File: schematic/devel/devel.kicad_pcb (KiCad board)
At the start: 2 copper layers, 66 parts, among them J1 CONN_PWR, J2 CONN_X1, J3 CONN_Y2, J4 CONN_X2, J5 CONN_Y1, Q1 Q_PMOS_GSD, Q2 Q_NMOS_GSD, Q3 Q_PMOS_GSD, Q4 Q_NMOS_GSD, U1 LM317_SOT223, U2 LM337_SOT223, U3 REF5010IDGK, U4 OPA4197

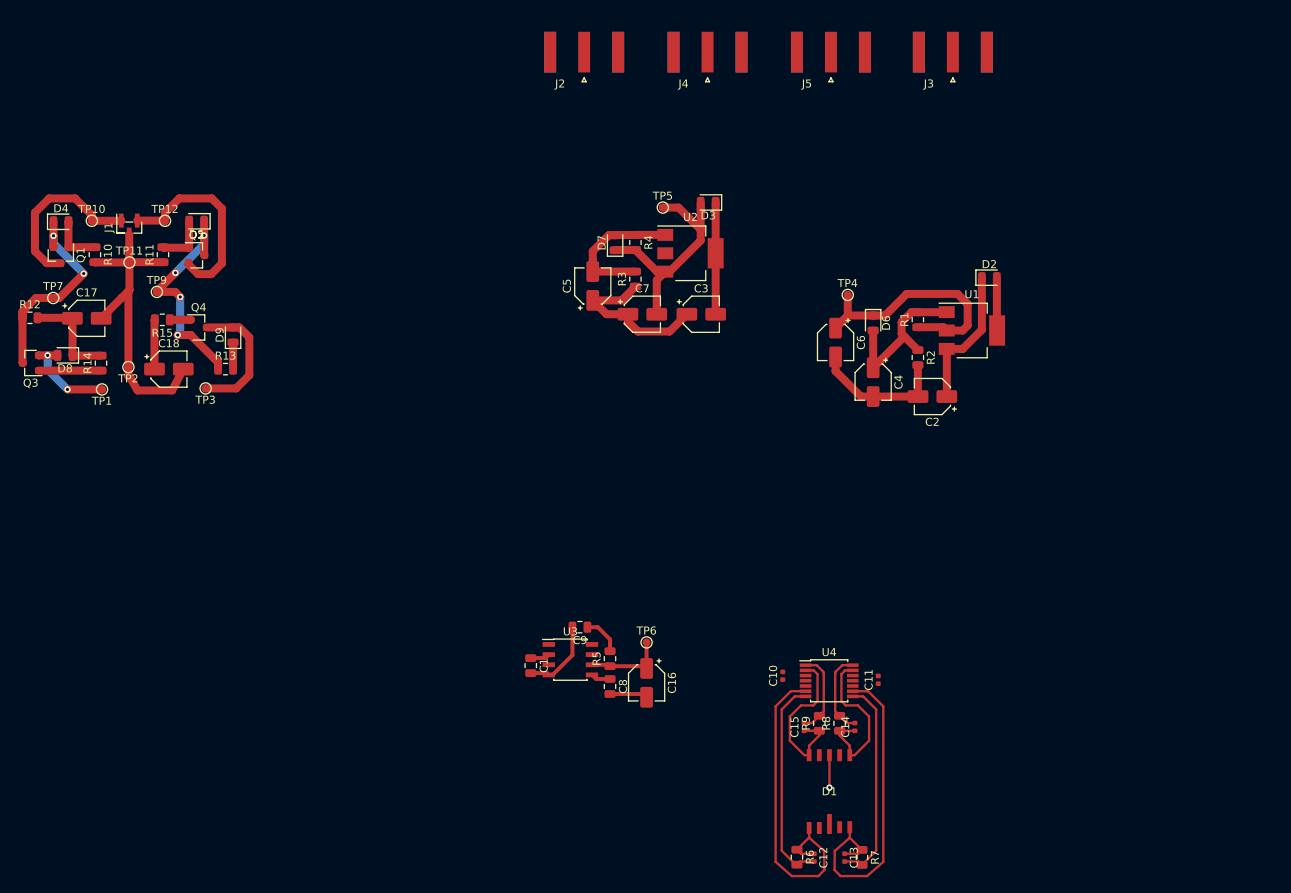
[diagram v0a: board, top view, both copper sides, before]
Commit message: retraced regulators according to datasheet layout
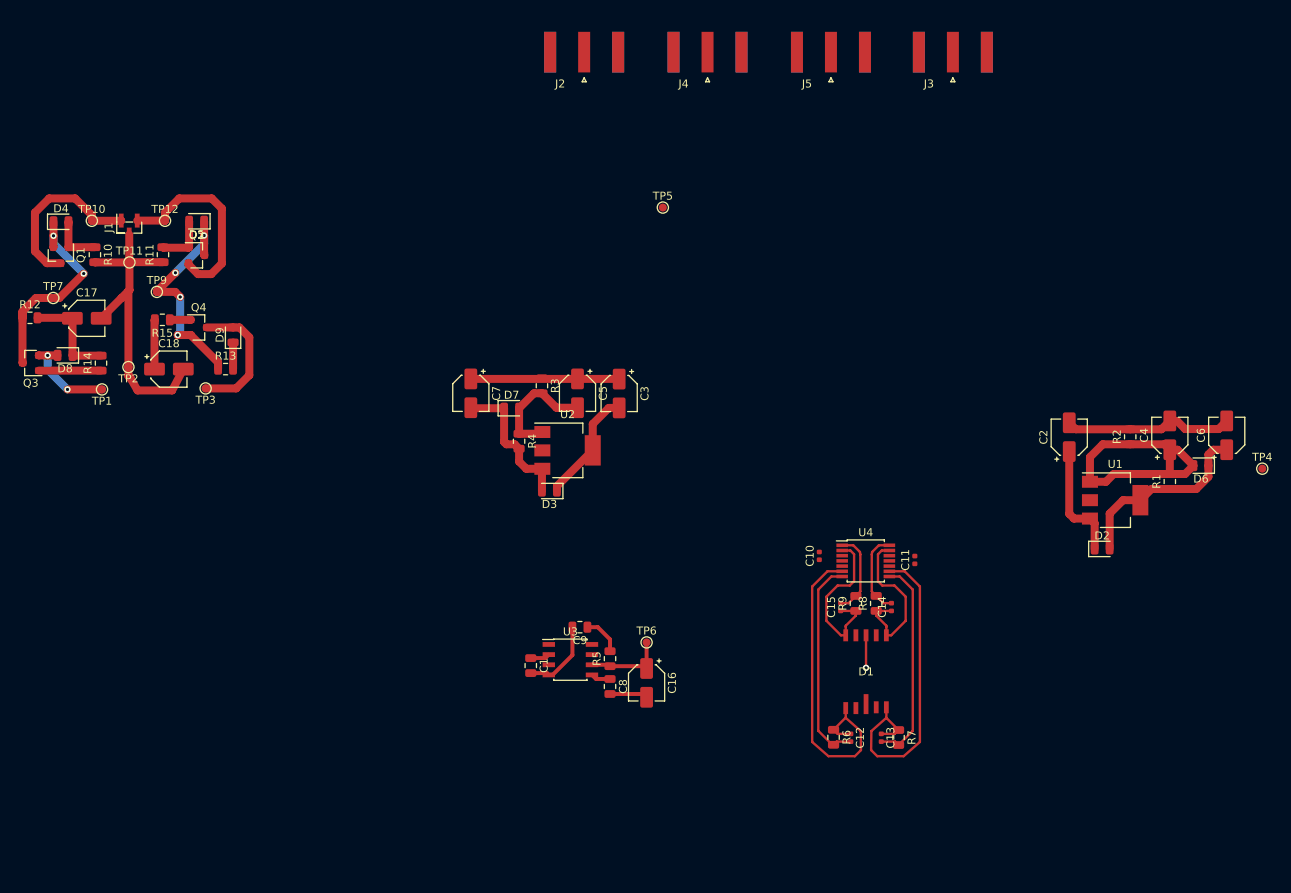
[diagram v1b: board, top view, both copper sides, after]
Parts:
- moved TP4 56.2 mm to (191.3, 125.2)
- moved C6 50.3 mm to (186.8, 121.1), turned to 90 degrees
- moved D6 44.7 mm to (183.6, 124.8), turned to 180 degrees
- moved D3 41.2 mm to (102.2, 128.0)
- moved C4 37.7 mm to (179.7, 121.1), turned to 90 degrees
- moved R1 37.4 mm to (179.7, 126.8)
- moved D2 36.7 mm to (171.2, 135.3)
- moved U2 29.0 mm to (104.4, 122.9)
- moved R4 28.8 mm to (98.4, 121.8)
- moved R2 28.3 mm to (174.8, 121.2), turned to 90 degrees
- moved U1 27.8 mm to (172.9, 129.2)
- moved D7 24.4 mm to (97.4, 117.7), turned to 0 degrees
- moved C7 23.6 mm to (92.3, 115.8), turned to 270 degrees
- moved C2 17.8 mm to (167.1, 121.3), turned to 90 degrees
- moved R3 17.7 mm to (101.2, 114.9), turned to 270 degrees
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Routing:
- net +12V: track 39.5 -> 24.0 mm
- net Net-(C4-Pad1): track 20.7 -> 34.6 mm
- net -12V: track 29.8 -> 18.3 mm
- net +15V: track 32.2 -> 29.0 mm
- net Net-(C5-Pad2): track 17.8 -> 15.0 mm
- net GND: track 93.9 -> 95.5 mm
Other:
- net class Default: clearance 0.1 -> 0.2
- rule trace_clearance: 0.1 -> 0.2

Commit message: moved sublayouts around
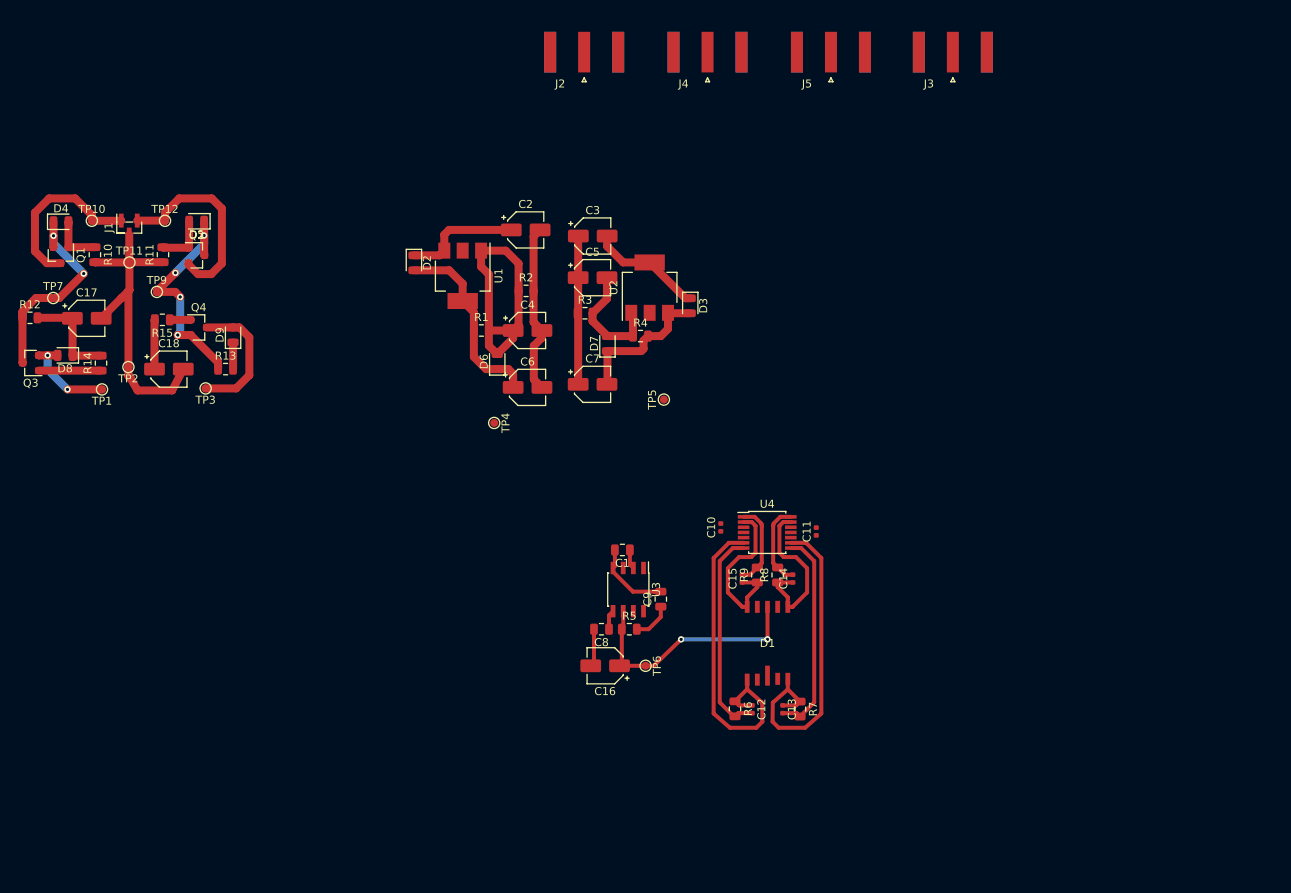
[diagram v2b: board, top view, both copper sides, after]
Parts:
- moved TP4 96.2 mm to (95.2, 119.5), turned to 270 degrees
- moved D2 93.2 mm to (85.2, 99.5), turned to 270 degrees
- moved D6 88.9 mm to (95.6, 111.8), turned to 90 degrees
- moved R1 88.1 mm to (93.6, 108.0), turned to 0 degrees
- moved C6 87.6 mm to (99.4, 115.1), turned to 0 degrees
- moved U1 86.2 mm to (91.3, 101.1), turned to 270 degrees
- moved C4 81.3 mm to (99.4, 108.0), turned to 0 degrees
- moved R2 77.7 mm to (99.2, 103.0), turned to 0 degrees
- moved C2 72.7 mm to (99.2, 95.4), turned to 0 degrees
- moved D3 29.1 mm to (119.8, 104.9), turned to 270 degrees
- moved TP5 24.0 mm to (116.5, 116.6), turned to 90 degrees
- moved U2 22.8 mm to (114.7, 102.6), turned to 90 degrees
- moved R4 20.1 mm to (113.5, 108.6), turned to 0 degrees
- moved C3 20.0 mm to (107.6, 96.1), turned to 0 degrees
- moved C1 18.4 mm to (111.3, 135.4), turned to 180 degrees
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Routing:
- net Net-(C16-Pad1): track 14.3 -> 31.0 mm, vias 1 -> 2

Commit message: created custom sma footprints
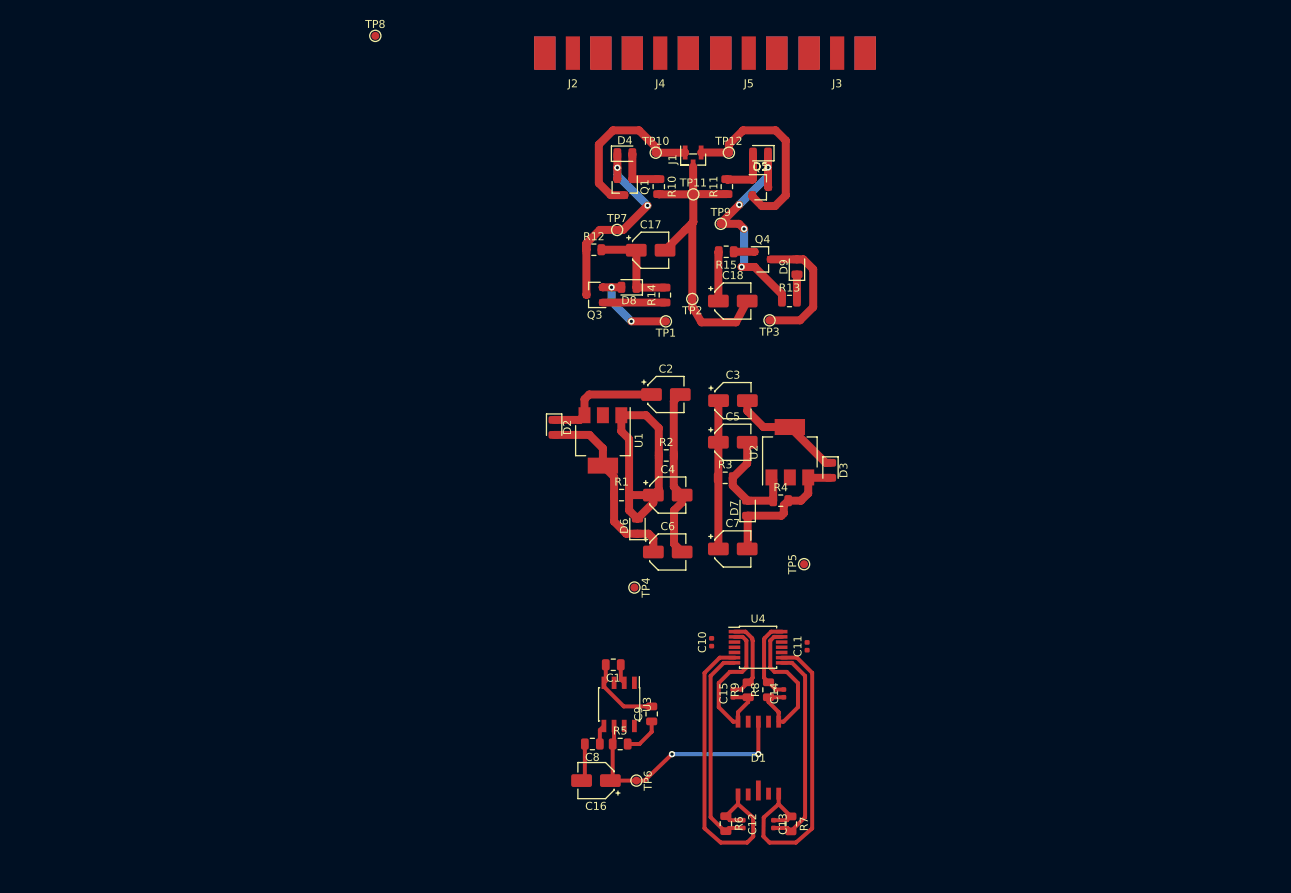
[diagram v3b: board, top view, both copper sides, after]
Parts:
- added TP8: TestPoint, TestPoint:TestPoint_Pad_D1.0mm, F.Cu at (80.4, 71.1)
- J2, J3, J4, J5: footprint Connector_Coaxial:SMA_Amphenol_132289_EdgeMount -> Connector_Coaxial_SMA:SMA_EdgeSlim
- moved C17 71.0 mm to (114.8, 97.9)
- moved D4 71.0 mm to (111.6, 85.9)
- moved D9 71.0 mm to (133.1, 100.0)
- moved J1 71.0 mm to (120.1, 86.6)
- moved Q4 71.0 mm to (128.8, 99.1)
- moved R13 71.0 mm to (132.2, 104.3)
- moved TP12 71.0 mm to (124.6, 85.7)
- moved TP7 71.0 mm to (110.6, 95.4)
- moved D8 71.0 mm to (112.1, 102.6)
- moved Q2 71.0 mm to (128.5, 90.0)
- moved Q3 71.0 mm to (107.8, 103.5)
- moved R10 71.0 mm to (115.8, 90.0)
- moved R11 71.0 mm to (124.3, 90.0)
- moved R12 71.0 mm to (107.7, 97.9)
- moved R14 71.0 mm to (116.6, 103.5)
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
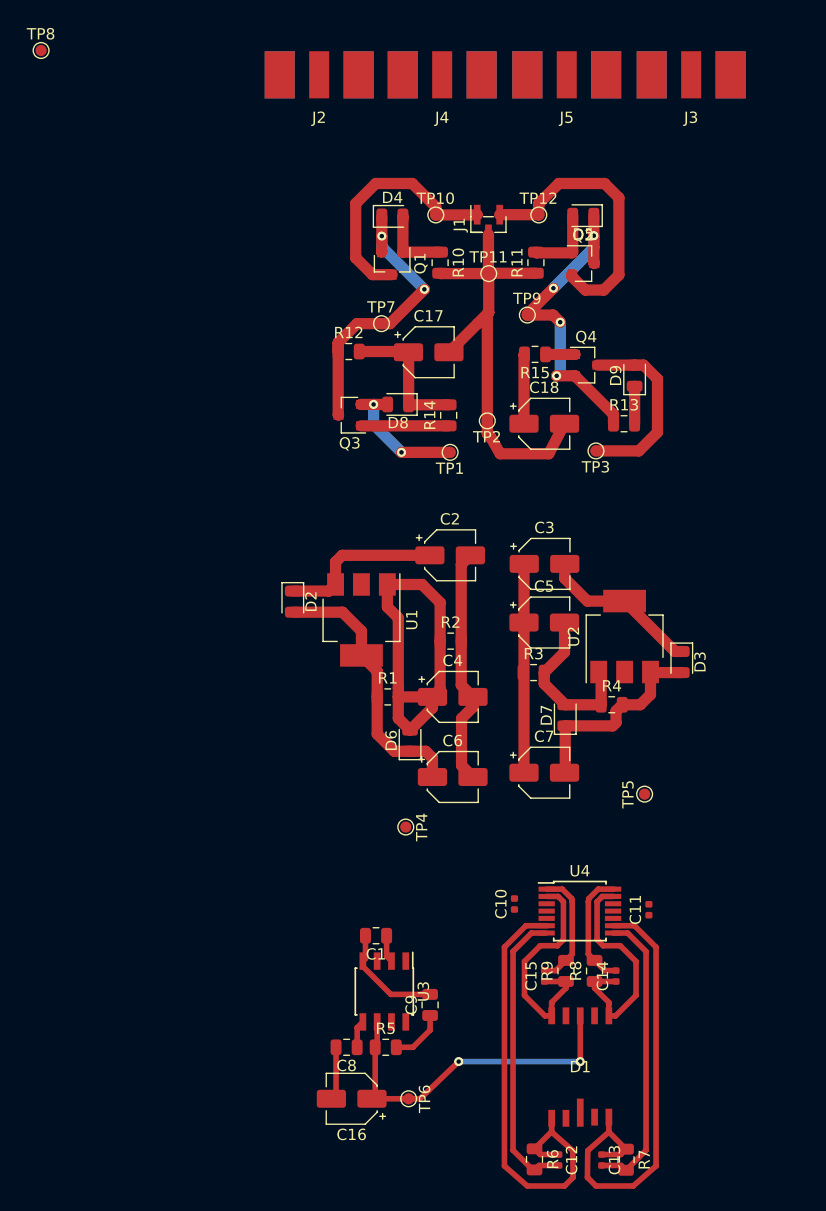
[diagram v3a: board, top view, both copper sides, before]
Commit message: completed pcb layout routing
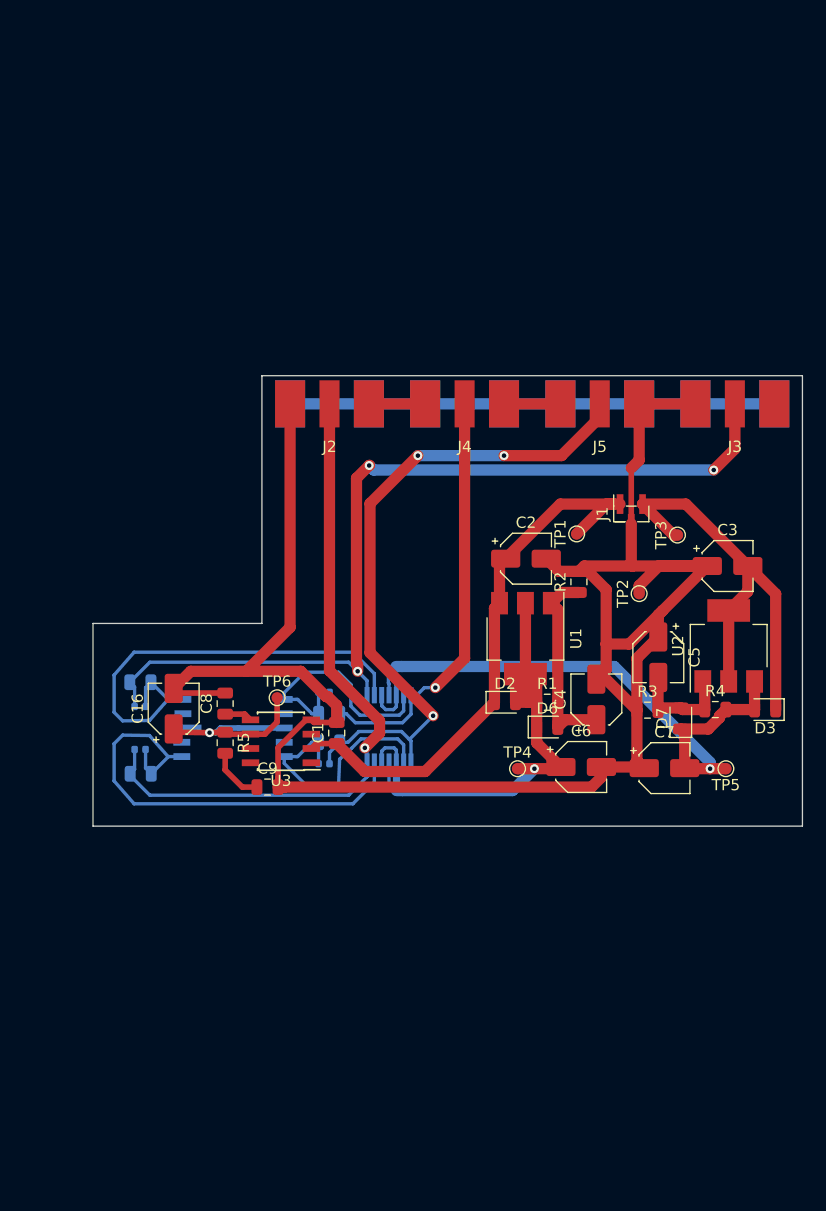
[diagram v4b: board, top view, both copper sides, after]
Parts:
- removed C17, C18: 100u, Capacitor_SMD:CP_Elec_4x3.9
- removed D4, D5: D_Zener_Small, Diode_SMD:D_0805_2012Metric
- removed D8, D9: D_Small, Diode_SMD:D_0805_2012Metric
- removed Q1, Q3: Q_PMOS_GSD, Package_TO_SOT_SMD:SOT-23
- removed Q2, Q4: Q_NMOS_GSD, Package_TO_SOT_SMD:SOT-23
- removed R10, R11: 100k, Resistor_SMD:R_0805_2012Metric
- removed R12, R13: 22, Resistor_SMD:R_0805_2012Metric
- removed R14, R15: 100, Resistor_SMD:R_0805_2012Metric
- removed TP10, TP11, TP12, TP7, TP8, TP9: TestPoint, TestPoint:TestPoint_Pad_D1.0mm
- C10, C11, C12, C13, C14, C15, D1, R6, R7, R8, R9, U4: moved to B.Cu
- moved R7 60.5 mm to (89.2, 127.2), turned to 180 degrees
- moved C13 57.5 mm to (89.2, 129.4), turned to 180 degrees
- moved C12 52.1 mm to (89.2, 133.2), turned to 180 degrees
- moved R6 48.9 mm to (89.2, 135.3), turned to 180 degrees
- moved D1 43.1 mm to (97.4, 131.3), turned to 90 degrees
- moved C16 38.1 mm to (92.2, 129.6), turned to 90 degrees
- moved TP6 37.5 mm to (101.3, 128.6), turned to 0 degrees
- moved C14 36.2 mm to (105.5, 128.1), turned to 0 degrees
- moved R8 32.8 mm to (106.0, 130.0), turned to 0 degrees
- moved C8 32.4 mm to (96.7, 129.1), turned to 90 degrees
- moved C11 30.8 mm to (111.9, 126.3)
- moved R5 30.6 mm to (96.7, 132.6), turned to 270 degrees
- moved J3 29.5 mm to (142.0, 102.5)
- moved J5 29.4 mm to (130.0, 102.5)
- moved J4 29.3 mm to (118.0, 102.5)
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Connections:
- J1 pad 1: Net-(J1-Pad1) -> +15V
- J1 pad 3: Net-(J1-Pad3) -> -15V
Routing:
- net GND: track 95.5 -> 238.7 mm
- net Net-(C13-Pad2): track 26.1 -> 82.3 mm, vias 0 -> 3
- net Net-(C15-Pad2): track 10.6 -> 60.1 mm, vias 0 -> 3
- net Net-(C12-Pad2): track 26.1 -> 60.3 mm, vias 0 -> 1
- net -12V: track 18.3 -> 52.2 mm, vias 0 -> 1
- net Net-(D5-Pad1): track 29.2 -> 0.00 mm, vias 4 -> 0
- net Net-(C14-Pad2): track 10.6 -> 39.7 mm, vias 0 -> 1
- net Net-(D4-Pad1): track 26.2 -> 0.00 mm, vias 2 -> 0
- net Net-(J1-Pad3): track 25.2 -> 0.00 mm
- net Net-(J1-Pad1): track 21.8 -> 0.00 mm
- net +15V: track 29.0 -> 49.7 mm, vias 2 -> 0
- net +12V: track 24.0 -> 43.2 mm, vias 0 -> 1
- net Net-(C4-Pad1): track 34.6 -> 17.8 mm
- net Net-(C17-Pad1): track 12.6 -> 0.00 mm
- net Net-(C16-Pad1): track 31.0 -> 18.8 mm, vias 2 -> 1
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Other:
- board outline added: 63 x 40 mm
- copper layers 2 -> 4
